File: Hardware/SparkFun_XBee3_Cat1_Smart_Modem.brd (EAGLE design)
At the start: 45.7 x 63.5 mm, 133 parts, among them J1 USB Female Type C Connector, J3 USB Female Type C Connector, J4 QWIIC_RIGHT_ANGLE, Q2 3.1A/30V/105mΩ, U1 FSUSB30MUX_MSOP10, U2 AP63203, U3 ESD Diode, U5 ESD Diode, U6 CP210X

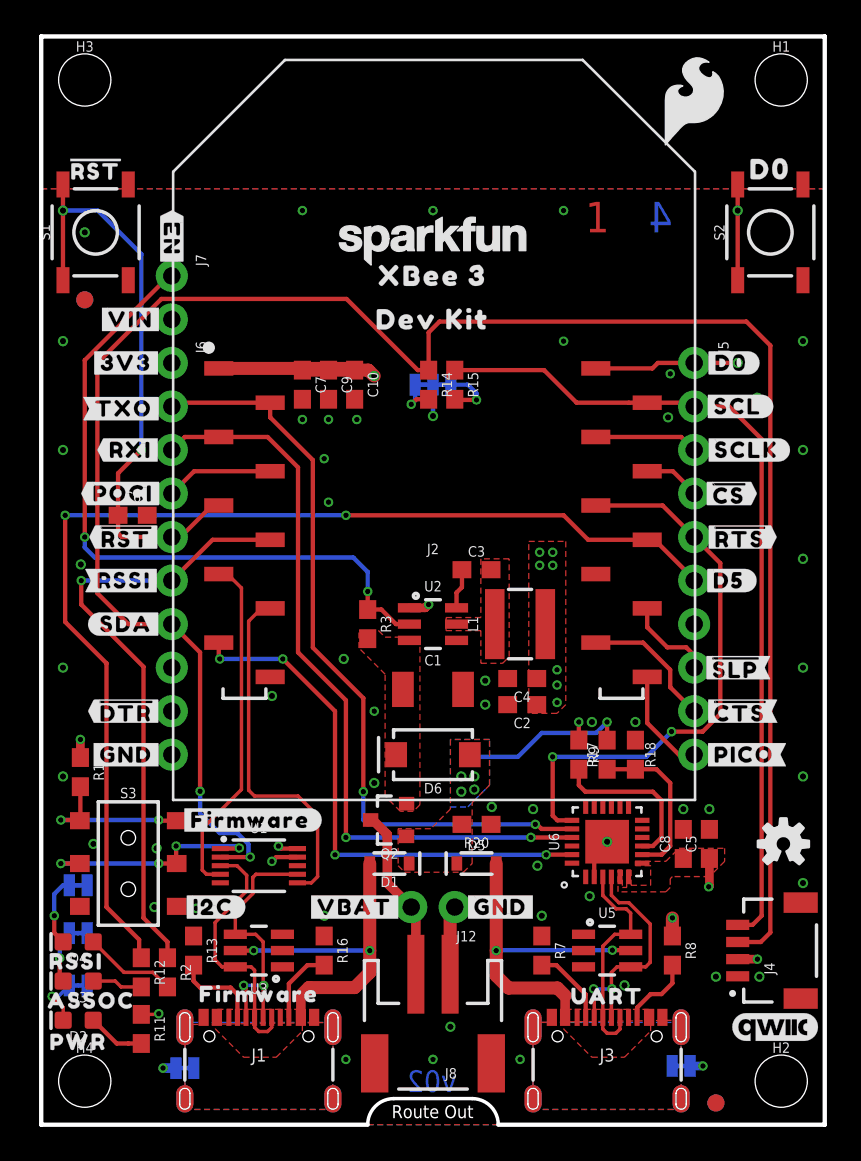
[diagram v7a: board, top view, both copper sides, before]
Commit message: Fixes silk on modem and silk for certain through holes
* Moves "VIN" and "EN" through holes
* Moves the switch down because the above through holes moved
* Shift the copper down to accommodate smaller XBee modules
* Changes name to "Development Board"
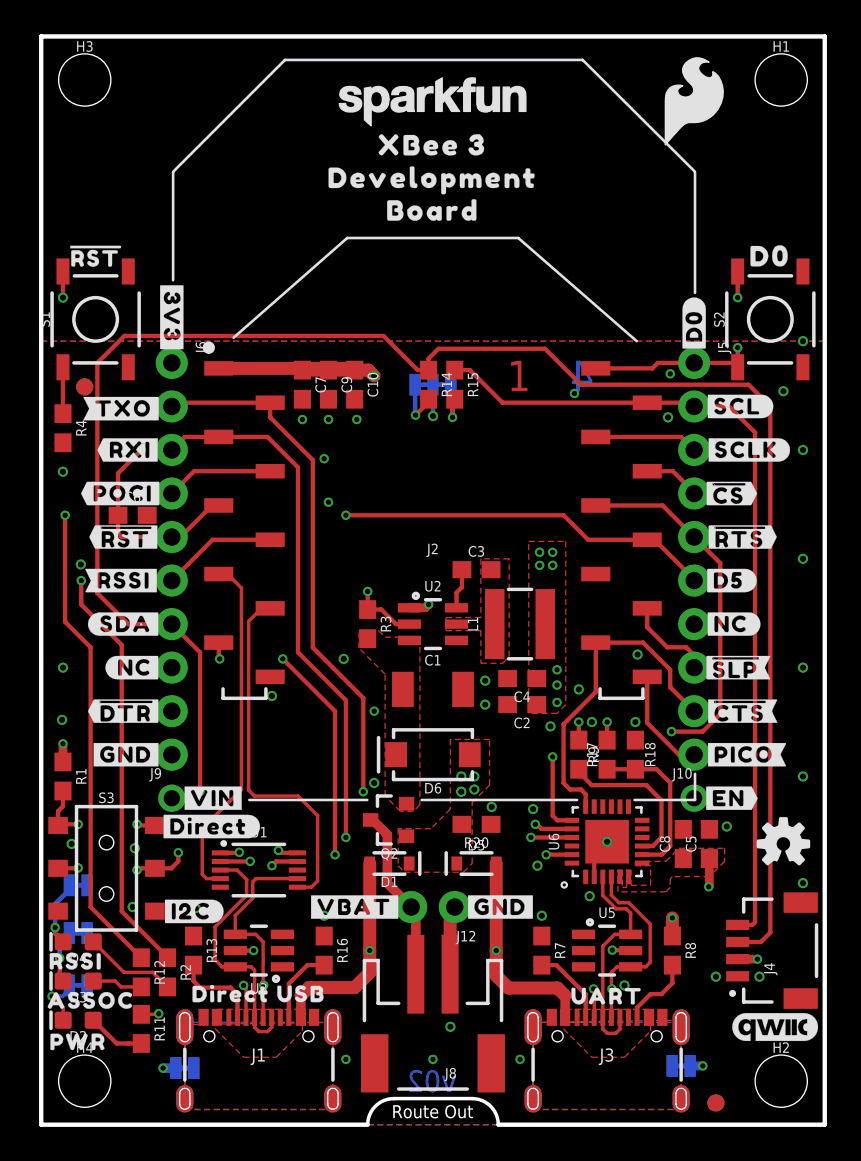
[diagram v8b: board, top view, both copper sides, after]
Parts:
- removed J7: (no value), SparkFun-Connectors:1X02_NO_SILK
- added J10, J9: (no value), SparkFun-Connectors:1X01_NO_SILK
- added R4: 10k, SparkFun-Resistors:0603
- added U$66: (no value), botmirror:#NC#3
- added U$67: (no value), topmirror:#NC#1
- added U$68: (no value), topmirror:DIRECT_USB33
- added U$69: (no value), botmirror:#DIRECT#31
- added U$70: (no value), topmirror:DEVELOPMENT1345
- added U$71: (no value), topmirror:BOARD1346
- J2: device xbee_smart_modem:XBEE3-SMD_SILK -> xbee_smart_modem:XBEE3-SMD
- U$21: device top:#EN#17 -> topmirror:#EN#17
- U$24: device top:#EN#17 -> topmirror:#NC#1
- U$48: device bot:#FIRMWARE#31 -> botmirror:#NC#3
- U$51: device top:DEV_KIT1340 -> topmirror:DEVELOPMENT1345
- U$52: device top:DEV_KIT1340 -> topmirror:BOARD1346
- U$8: device top:FIRMWARE29 -> topmirror:#EN#17
- moved U$21 40.3 mm to (36.1, 19.1)
- moved U$24 36.2 mm to (35.9, 29.2), flipped to the bottom, turned to 0 degrees
- moved U$8 29.7 mm to (40.1, 19.1)
- moved U$41 28.4 mm to (10.0, 19.1)
- moved U$46 27.9 mm to (10.0, 19.1)
- moved U$52 16.5 mm to (22.9, 53.3), flipped to the top
- moved U$48 9.21 mm to (9.78, 26.7), flipped to the bottom
- moved U$51 8.25 mm to (22.9, 55.2)
- moved LOGO1 8.13 mm to (22.9, 59.7)
- moved U$23 7.62 mm to (22.9, 57.1)
- moved FD1 5.08 mm to (2.54, 43.1)
- moved FD2 5.08 mm to (2.54, 43.1)
- moved S1 5.08 mm to (3.17, 47.0)
- moved S2 5.08 mm to (42.5, 47.0)
- moved U$30 5.08 mm to (3.17, 50.7)
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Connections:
- net !RESET!: now also R4.1
- net 3.3V: now also R4.2
- net D7/!CTS!: now also U6.18
- net EN: now also J10.1; no longer J7.1
- net VIN: now also J9.1; no longer J7.2
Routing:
- net VIN: track 52.2 -> 26.6 mm, vias 5 -> 6
- net D7/!CTS!: track 7.99 -> 19.2 mm
- net D0: track 22.9 -> 14.1 mm
- net D11/SDA: track 118.3 -> 112.3 mm
- net !RESET!: track 34.8 -> 30.1 mm
- net EN: track 40.1 -> 44.0 mm, vias 2 -> 1
- net FIRMWARE: track 10.0 -> 8.26 mm
- net DIRECT_SELECT: track 14.1 -> 12.6 mm
- net N$11: track 2.38 -> 3.03 mm
- net GND: vias 56 -> 53
- added copper zone on layer 15, net VIN
- removed copper zone on layer 16, net VIN
